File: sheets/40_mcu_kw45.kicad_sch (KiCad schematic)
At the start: 0 parts

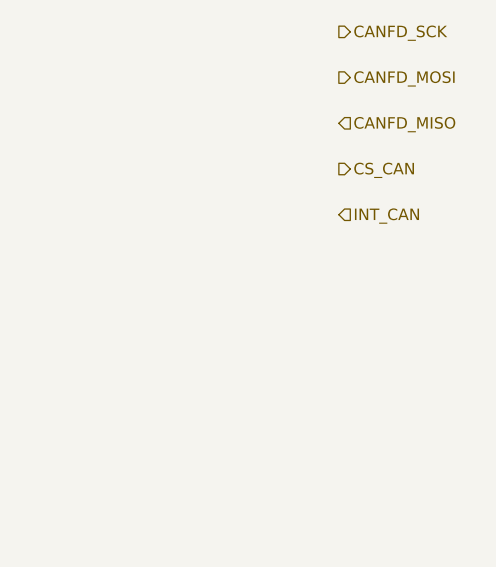
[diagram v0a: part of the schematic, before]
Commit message: Corrige la base del esquemático y añade reglas de proyecto
- Extrae el símbolo ADM3055E a lib/antmicro_adm3055ebriz.kicad_sym y lo
  registra en sym-lib-table con ${KIPRJMOD}.
- U1: huella Package_SO:SOIC-20W_7.5x12.8mm_P1.27mm (nota: verificar
  land pattern contra el datasheet).
- 10_power_input: power:GND -> GND_VEH; huellas y MPN de C1, C2 (0805
  X7R 100 V automotriz), C3 (EEE-HA2A470UP, 10x10) y F1 (1812, MPN
  pendiente).
- Nuevos pines jerárquicos CAN_SILENT (40_mcu -> 60_can, pull-down R1
  10k a GND_ISO) e IMU_INT2 (50_sensors -> 40_mcu).
- CLAUDE.md con reglas de librerías, campos, conexiones entre hojas,
  verificación por hoja y versión prototipo.
- Ignora output/ (reportes generados por kicad-mcp).

Co-Authored-By: Claude Opus 5.5 <noreply@anthropic.com>
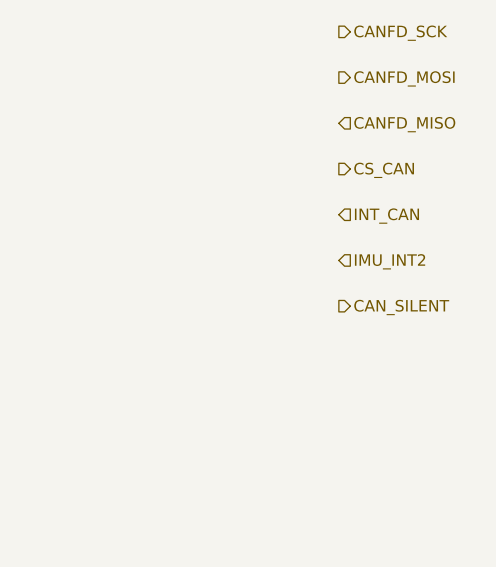
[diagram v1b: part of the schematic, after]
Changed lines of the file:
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@@
+		)
+	)
+	(hierarchical_label "IMU_INT2"
+		(shape input)
+		(at 375.92 106.68 0)
+		(effects
+			(font
+				(size 1.27 1.27)
+			)
+			(justify left)
+		)
+	)
+	(hierarchical_label "CAN_SILENT"
+		(shape output)
+		(at 375.92 111.76 0)
+		(effects
+			(font
+				(size 1.27 1.27)
+			)
+			(justify left)
 		)
 	)

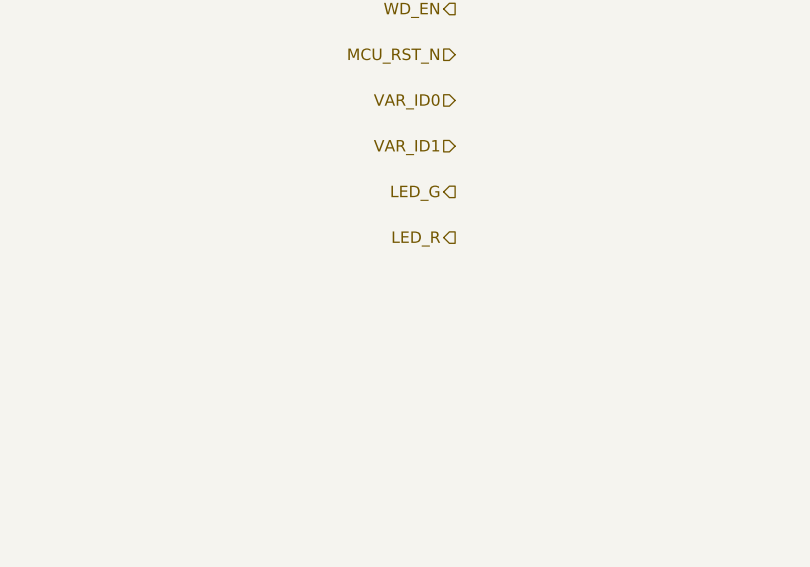
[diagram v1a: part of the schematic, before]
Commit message: 70_output: salida low-side con latch y señal PWR_FLT
- 70_output (DO1/DO2): MOSFET FDD7N25LZ (demo, 250 V) con TVS SMCJ188A
  en el drenador, latch de sobrecorriente a ~0.7 A (R 1 ohm + BC817/BC807,
  rearme con EN=0), apagado del gate por PWR_FLT_N o latch (BAT54A) y
  DIAG por divisor del drenador con zener 5V1. OUT pasa a pasivo.
- Jerarquía: VEH_PWR_FLT_N de 10_power_input a 70_output y 20_isolation;
  PWR_FLT de 20_isolation a 40_mcu (KW45 y ESP32-S3).
- 10_power_input: solo interfaz (VEH_DO1/2 pasivos, VEH_PWR_FLT_N);
  el circuito con LM74930 va en un commit aparte.
- CLAUDE.md: procedimiento para componentes fuera de las librerías.
- README: 70_output es low-side.

Co-Authored-By: Claude Opus 5.5 <noreply@anthropic.com>
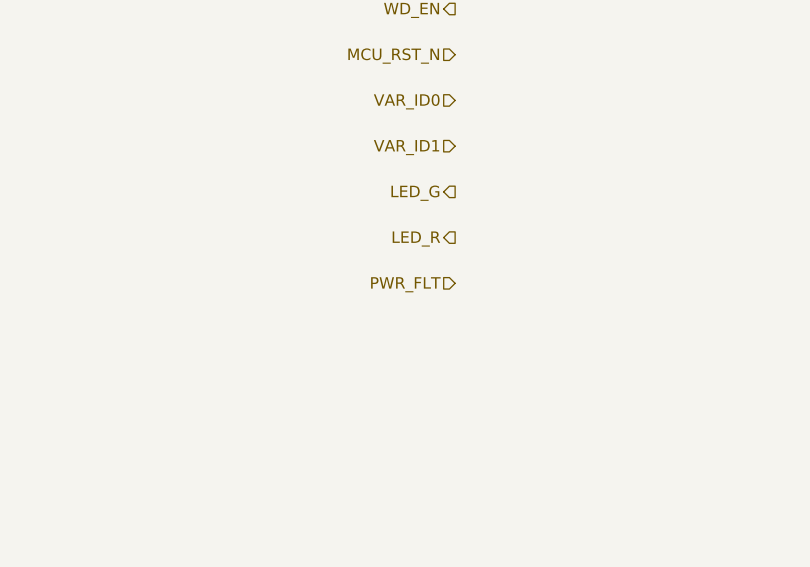
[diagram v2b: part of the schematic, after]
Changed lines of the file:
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@@
+		)
+	)
+	(hierarchical_label "PWR_FLT"
+		(shape input)
+		(at 238.76 96.52 180)
+		(effects
+			(font
+				(size 1.27 1.27)
+			)
+			(justify right)
 		)
 	)

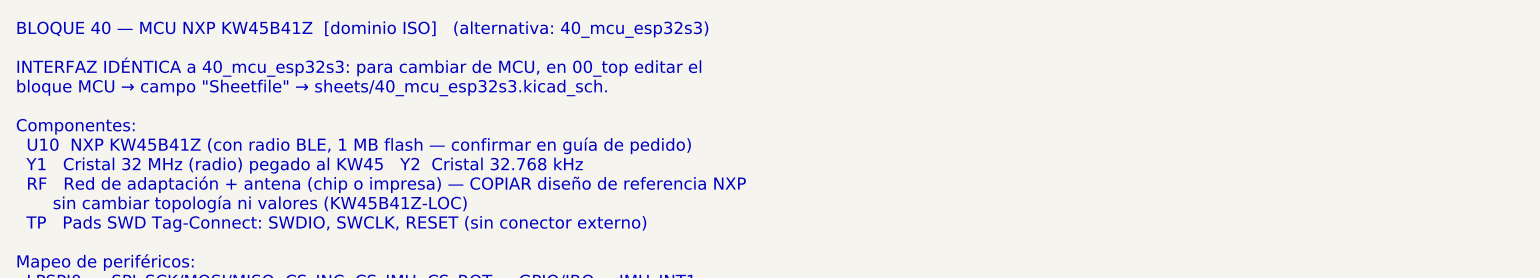
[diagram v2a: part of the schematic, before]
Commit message: Alcance: solo ESP32-S3, CAN clásico por TWAI, sin MCP2518FD
- Raíz: el bloque 40_mcu apunta a 40_mcu_esp32s3. 40_mcu_kw45 queda en
  el repo solo como referencia, fuera de la jerarquía.
- CAN: se eliminan el MCP2518FD, el cristal y los pines CANFD_SCK/MOSI/
  MISO, CS_CAN e INT_CAN en 60_can, 40_mcu_esp32s3 y la raíz (etiquetas,
  cables y pines de hoja). TWAI nativo (J1939) directo al ADM3055E.
  Se quita la variante CANFD.
- 20_isolation (nota): PS1 >= 5 W y entrada 9-72 V (corte OV 38.4 V);
  U2 = TPS7A1650-Q1 para +5V_VEH.
- 40_mcu_esp32s3 (nota): desacople 22 uF + 100 nF según Espressif y
  límite de 47 uF en +3V3_D por el TPS62A02-Q1; solo BLE en operación.
- README: tabla corregida (LM74930-Q1 en 10_power_input, 20, 30, 40, 60),
  sección MCU y "Requisitos para el firmware" (rearme del latch >= 100 ms,
  arranque limpio tras brownout, NimBLE con WiFi desactivado).
- CLAUDE.md: sección "Alcance" (ESP32-S3 único, dimensionar con WiFi).

ERC: 180 -> 160 violaciones; sin errores nuevos. Las restantes son de
hojas sin terminar (20, 30, 60) y etiquetas de la raíz sin destino.

Co-Authored-By: Claude Opus 5.5 <noreply@anthropic.com>
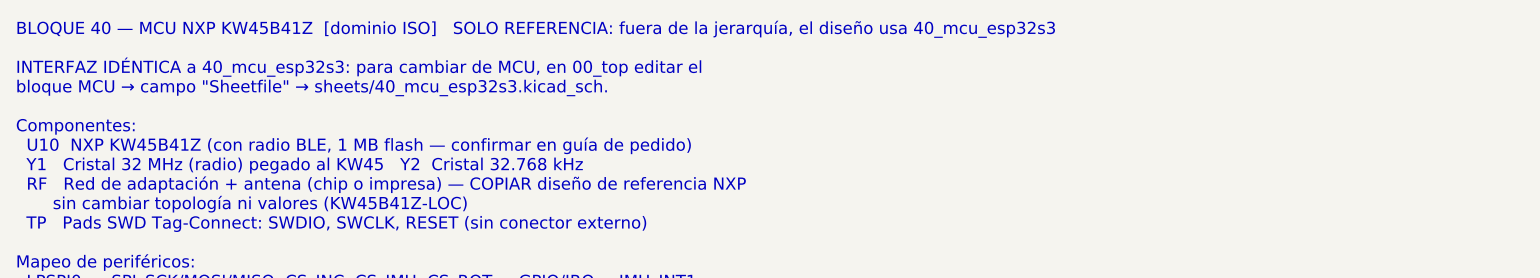
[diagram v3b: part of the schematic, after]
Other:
- note added: "BLOQUE 40 — MCU NXP KW45B41Z [dominio ISO] SOLO REFERENCIA: fuera de la jerarquía, el diseño usa 40_mcu_esp32s3 INTERFAZ IDÉNTICA a 40_mcu_esp32s3: para cambiar de MCU, en 00_top editar el bloque MCU → campo "Sheetfile" → sheets/40_mcu_esp32s3.kicad_sch. Componentes: U10 NXP KW45B41Z (con radio BLE, 1 MB flash — confirmar en guía de pedido) Y1 Cristal 32 MHz (radio) pegado al KW45 Y2 Cristal 32.7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"
- note removed: "BLOQUE 40 — MCU NXP KW45B41Z [dominio ISO] (alternativa: 40_mcu_esp32s3) INTERFAZ IDÉNTICA a 40_mcu_esp32s3: para cambiar de MCU, en 00_top editar el bloque MCU → campo "Sheetfile" → sheets/40_mcu_esp32s3.kicad_sch. Componentes: U10 NXP KW45B41Z (con radio BLE, 1 MB flash — confirmar en guía de pedido) Y1 Cristal 32 MHz (radio) pegado al KW45 Y2 Cristal 32.768 kHz RF Red de adaptación + antena (c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"
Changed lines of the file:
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@@
 		)
 	)
-	(text "BLOQUE 40 — MCU NXP KW45B41Z  [dominio ISO]   (alternativa: 40_mcu_esp32s3)\n\nINTERFAZ IDÉNTICA a 40_mcu_esp32s3: para cambiar de MCU, en 00_top editar el\nbloque MCU → campo \"Sheetfile\" → sheets/40_mcu_esp32s3.kicad_sch.\n\nComponentes:\n  U10  NXP KW45B41Z (con radio BLE, 1 MB flash — confirmar en guía de pedido)\n  Y1   Cristal 32 MHz (radio) pegado al KW45   Y2  Cristal 32.768 kHz\n  RF   Red de adaptación + antena (chip o impresa) — COPIAR diseño de referencia NXP\n       sin cambiar topología ni valores (KW45B41Z-LOC)\n  TP   Pads SWD Tag-Connect: SWDIO, SWCLK, RESET (sin conector externo)\n\nMapeo de periféricos:\n  LPSPI0  → SPI_SCK/MOSI/MISO, CS_INC, CS_IMU, CS_ROT     GPIO/IRQ ← IMU_INT1\n  FlexCAN0 → CAN_TX, CAN_RX (CAN FD nativo)              GPIO → CAN_STBY\n  CANFD_SCK/MOSI/MISO, CS_CAN, INT_CAN: NO SE USAN con KW45 → poner No-Connect\n  GPIO → DO1_EN, DO2_EN (alto = salida activa)  ← DO1_DIAG, DO2_DIAG\n  GPIO → WDI, WD_EN   ← MCU_RST_N (desde TPS3431)\n  ADC  ← VMON_5V, VMON_3V3     GPIO ← VAR_ID0/1    GPIO → LED_G, LED_R\nAsignación exacta de pines con MCUXpresso Config Tools (conflictos con la radio).\nDesacople de cada pin VDD junto al pin, con valor y encapsulado."
+	(text "BLOQUE 40 — MCU NXP KW45B41Z  [dominio ISO]   SOLO REFERENCIA: fuera de la jerarquía, el diseño usa 40_mcu_esp32s3\n\nINTERFAZ IDÉNTICA a 40_mcu_esp32s3: para cambiar de MCU, en 00_top editar el\nbloque MCU → campo \"Sheetfile\" → sheets/40_mcu_esp32s3.kicad_sch.\n\nComponentes:\n  U10  NXP KW45B41Z (con radio BLE, 1 MB flash — confirmar en guía de pedido)\n  Y1   Cristal 32 MHz (radio) pegado al KW45   Y2  Cristal 32.768 kHz\n  RF   Red de adaptación + antena (chip o impresa) — COPIAR diseño de referencia NXP\n       sin cambiar topología ni valores (KW45B41Z-LOC)\n  TP   Pads SWD Tag-Connect: SWDIO, SWCLK, RESET (sin conector externo)\n\nMapeo de periféricos:\n  LPSPI0  → SPI_SCK/MOSI/MISO, CS_INC, CS_IMU, CS_ROT     GPIO/IRQ ← IMU_INT1\n  FlexCAN0 → CAN_TX, CAN_RX (CAN FD nativo)              GPIO → CAN_STBY\n  CANFD_SCK/MOSI/MISO, CS_CAN, INT_CAN: NO SE USAN con KW45 → poner No-Connect\n  GPIO → DO1_EN, DO2_EN (alto = salida activa)  ← DO1_DIAG, DO2_DIAG\n  GPIO → WDI, WD_EN   ← MCU_RST_N (desde TPS3431)\n  ADC  ← VMON_5V, VMON_3V3     GPIO ← VAR_ID0/1    GPIO → LED_G, LED_R\nAsignación exacta de pines con MCUXpresso Config Tools (conflictos con la radio).\nDesacople de cada pin VDD junto al pin, con valor y encapsulado."
 		(exclude_from_sim no)
 		(at 20.32 20.32 0)
@@
 		)
 	)
+	(hierarchical_label "PWR_FLT"
+		(shape input)
+		(at 238.76 96.52 180)
+		(effects
+			(font
+				(size 1.27 1.27)
+			)
+			(justify right)
+		)
+	)
 	(hierarchical_label "LED_R"
 		(shape output)
@@
 		)
 	)
+	(hierarchical_label "CAN_SILENT"
+		(shape output)
+		(at 375.92 111.76 0)
+		(effects
+			(font
+				(size 1.27 1.27)
+			)
+			(justify left)
+		)
+	)
 	(hierarchical_label "IMU_INT1"
 		(shape input)
@@
 		(shape input)
 		(at 375.92 101.6 0)
+		(effects
+			(font
+				(size 1.27 1.27)
+			)
+			(justify left)
+		)
+	)
+	(hierarchical_label "IMU_INT2"
+		(shape input)
+		(at 375.92 106.68 0)
 		(effects
 			(font
@@
 		)
 	)
-	(hierarchical_label "IMU_INT2"
-		(shape input)
-		(at 375.92 106.68 0)
-		(effects
-			(font
-				(size 1.27 1.27)
-			)
-			(justify left)
-		)
-	)
-	(hierarchical_label "CAN_SILENT"
-		(shape output)
-		(at 375.92 111.76 0)
-		(effects
-			(font
-				(size 1.27 1.27)
-			)
-			(justify left)
-		)
-	)
-	(hierarchical_label "PWR_FLT"
-		(shape input)
-		(at 238.76 96.52 180)
-		(effects
-			(font
-				(size 1.27 1.27)
-			)
-			(justify right)
-		)
-	)
